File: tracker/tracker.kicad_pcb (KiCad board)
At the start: 4 copper layers, 49.4 x 53.2 mm, 88 parts, among them J1 Conn_01x01, J2 Conn_01x01, J3 Conn_01x05, J4 Conn_Coaxial, J5 SIM_Card, J6 Conn_01x02, M1 BG96, Q1 DMP2008UFG, U1 STM32U545CEUx, U10 PUMH10,115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

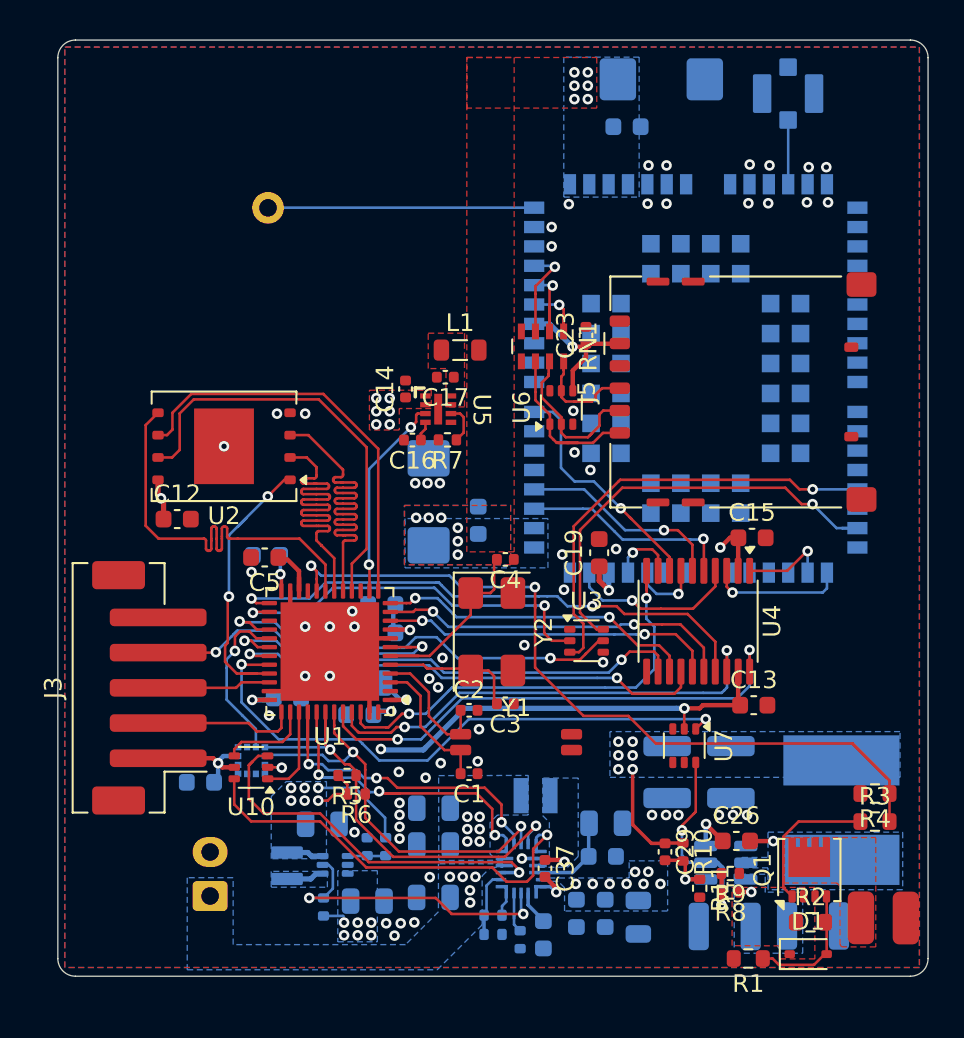
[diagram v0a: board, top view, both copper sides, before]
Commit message: edit silkscreen
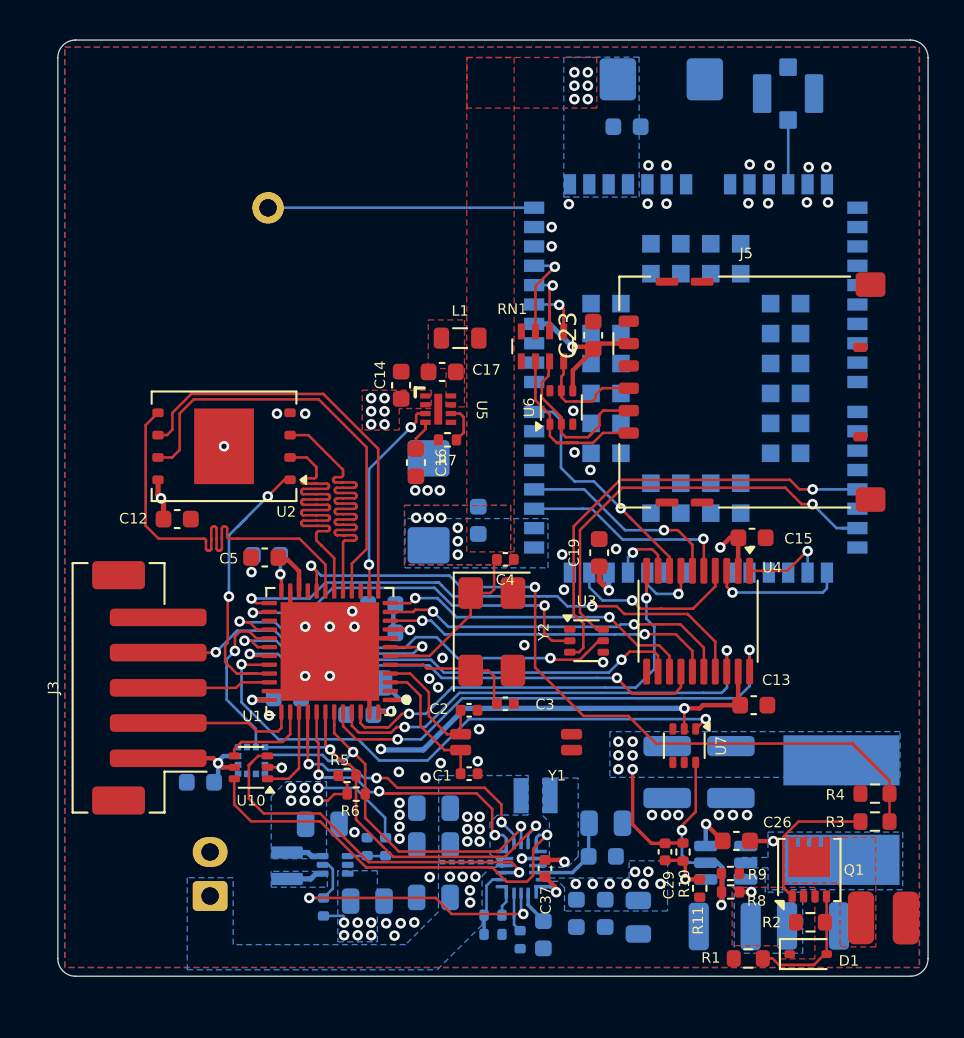
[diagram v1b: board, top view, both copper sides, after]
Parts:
- C14, C16, C17, C23: footprint Capacitor_SMD:C_0402_1005Metric -> Capacitor_SMD:C_0603_1608Metric
- moved C16 1.30 mm to (142.9, 67.4), turned to -90 degrees
- moved L1 0.68 mm to (145.4, 60.3)
- moved J5 0.51 mm to (161.6, 63.4)
- moved C23 0.41 mm to (153.0, 60.1)
- moved C17 0.35 mm to (144.4, 62.2)
- moved C14 0.33 mm to (142.1, 63.0)
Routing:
- net Net-(U5-SS): track 1.11 -> 2.11 mm

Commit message: edits
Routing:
- net /mcu/VIN_MEAS: track 47.2 -> 44.2 mm
- net /battery charger/CHARGER_INT: track 19.6 -> 17.4 mm
- net /mcu/OSC_OUT: track 11.7 -> 10.1 mm
- net /gsm/SIM_IO: track 5.23 -> 3.75 mm
- net /battery charger/CHARGER_STAT: track 18.7 -> 17.3 mm
- net Net-(J5-CLK): track 10.2 -> 8.95 mm
- net /I2C_SCL: track 25.3 -> 24.0 mm
- net /gsm/GSM_LINE_BUF_EN: track 25.7 -> 24.6 mm
- net /gsm/SIM_RST: track 4.02 -> 3.04 mm
- net /mcu/OCTOSPI1_NCS: track 16.7 -> 15.8 mm
- net /mcu/VCAP: track 2.86 -> 2.08 mm
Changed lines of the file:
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@@
 	)
 	(paper "A4")
+	(title_block
+		(date "2025-10-27")
+	)
 	(layers
 		(0 "F.Cu" signal)
@@
 		(tags "resistor")
 		(property "Reference" "R7"
-			(at 0 -1.17 0)
+			(at -1.46 -0.13 0)
 			(layer "F.SilkS")
 			(effects
@@
 		(tags "capacitor")
 		(property "Reference" "C23"
-			(at 0 -1.43 90)
+			(at 1.26 -0.91 90)
 			(layer "F.SilkS")
 			(effects
 				(font
-					(size 1 1)
+					(size 0.6 0.6)
 					(thickness 0.15)
 				)
@@
 		(tags "capacitor")
 		(property "Reference" "C16"
-			(at 0 -1.43 90)
+			(at 0 1.08 90)
 			(layer "F.SilkS")
 			(effects
@@
 		(tags "connector JST PH vertical")
 		(property "Reference" "J3"
-			(at 0 -5.45 90)
+			(at 7.905 -3.44 180)
 			(layer "F.SilkS")
 			(effects
@@
 		(tags "capacitor")
 		(property "Reference" "C4"
-			(at 0 -1.16 0)
+			(at -0.112 0.998 0)
 			(layer "F.SilkS")
 			(effects
@@
 		(tags "Inductor")
 		(property "Reference" "L2"
-			(at 0.1 5.4 90)
+			(at 5.16 0.41 180)
 			(layer "B.SilkS")
 			(effects
@@
 	)
 	(segment
-		(start 141.4375 78.3625)
-		(end 143.05 78.3625)
-		(width 0.15)
-		(layer "F.Cu")
-		(net 5)
-	)
-	(segment
 		(start 147.33 73.04)
 		(end 147.33 74.58)
@@
 	)
 	(segment
-		(start 142.34 77.8625)
-		(end 142.6375 77.8625)
-		(width 0.15)
-		(layer "F.Cu")
-		(net 12)
-	)
-	(segment
 		(start 131.5 78.175)
 		(end 131.525 78.15)
@@
 	(segment
 		(start 150.48 59.93)
-		(end 150.48 58.45)
-		(width 0.15)
-		(layer "F.Cu")
-		(net 17)
-	)
-	(segment
-		(start 150.48 59.93)
 		(end 150.48 57.5)
 		(width 0.15)
@@
 	)
 	(segment
-		(start 155.05 70.5)
-		(end 155.125 70.575)
-		(width 0.15)
-		(layer "F.Cu")
-		(net 34)
-	)
-	(segment
 		(start 154.525 69.975)
 		(end 155.05 70.5)
@@
 	(segment
 		(start 158.16 71.75)
-		(end 158.47 71.75)
-		(width 0.15)
-		(layer "B.Cu")
-		(net 45)
-	)
-	(segment
-		(start 158.16 71.75)
 		(end 159.18 71.75)
 		(width 0.15)
@@
 	(segment
 		(start 151.28 59.93)
-		(end 151.28 58.954166)
-		(width 0.15)
-		(layer "F.Cu")
-		(net 75)
-	)
-	(segment
-		(start 151.28 59.93)
 		(end 151.28 58.672)
 		(width 0.15)
@@
 	)
 	(segment
-		(start 169.65 85.3)
-		(end 167.69 83.34)
-		(width 0.15)
-		(layer "F.Cu")
-		(net 86)
-	)
-	(segment
 		(start 156.52 83.34)
 		(end 154.95 81.77)
@@
 	)
 	(segment
-		(start 149.66 75.63)
-		(end 149.66 75.45)
-		(width 0.15)
-		(layer "F.Cu")
-		(net 86)
-	)
-	(segment
 		(start 149.66 74.7)
 		(end 149.64 74.68)
@@
 	)
 	(segment
-		(start 133.55 79.3625)
-		(end 133.2875 79.3625)
-		(width 0.15)
-		(layer "F.Cu")
-		(net 89)
-	)
-	(segment
 		(start 132.051 78.701)
 		(end 132.051 77.77)
@@
 	)
 	(segment
-		(start 132.775 71.025)
-		(end 133.25 70.55)
-		(width 0.15)
-		(layer "B.Cu")
-		(net 89)
-	)
-	(segment
 		(start 132.27 74.99)
 		(end 132.27 71.505)
@@
 	)
 	(segment
-		(start 137.51 72.07)
-		(end 137.54 72.1)
-		(width 0.15)
-		(layer "F.Cu")
-		(net 91)
-	)
-	(segment
 		(start 137.24 69.175015)
 		(end 136.5 69.175015)
@@
 	)
 	(segment
-		(start 145.08 76.05)
-		(end 144.96 75.93)
-		(width 0.15)
-		(layer "B.Cu")
-		(net 100)
-	)
-	(segment
-		(start 144.96 75.93)
-		(end 144.27 75.24)
-		(width 0.15)
-		(layer "B.Cu")
-		(net 100)
-	)
-	(segment
 		(start 145.19 76.16)
-		(end 144.96 75.93)
+		(end 153.88 76.16)
 		(width 0.15)
 		(layer "B.Cu")
@@
 	)
 	(segment
-		(start 144.11 75.08)
-		(end 142.85 75.08)
+		(start 142.85 75.08)
+		(end 144.11 75.08)
 		(width 0.15)
 		(layer "B.Cu")
@@
 	)
 	(segment
-		(start 153.88 76.16)
+		(start 144.11 75.08)
 		(end 145.19 76.16)
 		(width 0.15)
@@
 	)
 	(segment
-		(start 144.27 75.24)
-		(end 144.11 75.08)
-		(width 0.15)
-		(layer "B.Cu")
-		(net 100)
-	)
-	(segment
 		(start 161.845 79.2525)
 		(end 161.845 78.025)
@@
 	(segment
 		(start 155.995 73.5275)
-		(end 155.995 74.63)
-		(width 0.15)
-		(layer "F.Cu")
-		(net 103)
-	)
-	(segment
-		(start 155.995 73.5275)
 		(end 155.995 75.065)
 		(width 0.15)
@@
 	)
 	(segment
-		(start 144.195 74.195)
-		(end 144.024678 74.195)
-		(width 0.15)
-		(layer "B.Cu")
-		(net 104)
-	)
-	(segment
 		(start 156.87 76.57)
 		(end 157.915 76.57)
@@
 	)
 	(segment
-		(start 141.95 86.17)
-		(end 141.16 86.17)
-		(width 0.15)
-		(layer "F.Cu")
-		(net 108)
-	)
-	(segment
 		(start 146.34 86.17)
 		(end 141.95 86.17)
@@
 	)
 	(segment
-		(start 137.73 85.28)
-		(end 138.32 85.28)
-		(width 0.15)
-		(layer "B.Cu")
-		(net 108)
-	)
-	(segment
 		(start 137.36 85.11)
 		(end 137.53 85.28)
@@
 	)
 	(segment
-		(start 136.75 81.55)
-		(end 136.75 83.7)
-		(width 0.15)
-		(layer "F.Cu")
-		(net 110)
-	)
-	(segment
 		(start 141.83 85.85)
 		(end 146.8 85.85)
@@
 	)
 	(segment
-		(start 136.25 74.675)
-		(end 136.25 73.9)
-		(width 0.254)
-		(layer "F.Cu")
-		(net 118)
-	)
-	(segment
 		(start 136.25 73.545)
 		(end 135.575 72.87)
@@
 	)
 	(segment
-		(start 151.895001 63.91)
-		(end 151.98 63.91)
-		(width 0.15)
-		(layer "F.Cu")
-		(net 127)
-	)
-	(segment
 		(start 153.1025 63.5125)
 		(end 153.46 63.155)
@@
 	)
 	(segment
-		(start 150.95 66.26)
-		(end 151.59 66.26)
-		(width 0.15)
-		(layer "F.Cu")
-		(net 129)
-	)
-	(segment
 		(start 150.5 65.2)
 		(end 150.5 64.66)
@@
 	)
 	(segment
-		(start 151.46 66.26)
-		(end 151.59 66.26)
-		(width 0.15)
-		(layer "F.Cu")
-		(net 129)
-	)
-	(segment
 		(start 150.5 65.87)
 		(end 150.7 66.07)
@@
 	)
 	(segment
-		(start 151.59 66.26)
-		(end 152.08 66.26)
-		(width 0.15)
-		(layer "F.Cu")
-		(net 129)
-	)
-	(segment
 		(start 152.08 66.26)
 		(end 152.95 66.26)
@@
 	)
 	(segment
-		(start 137.75 82.81)
-		(end 137.75 81.55)
-		(width 0.15)
-		(layer "F.Cu")
-		(net 132)
-	)
-	(segment
 		(start 149.71 88.01)
 		(end 147.945 89.775)
@@
 	)
 	(segment
-		(start 148.463 93.11)
-		(end 148.463 93.287)
-		(width 0.15)
-		(layer "B.Cu")
-		(net 137)
-	)
-	(segment
 		(start 148.463 93.623)
 		(end 148.81 93.97)
@@
 	)
 	(segment
-		(start 133.4 86.47)
-		(end 133.4 84.57)
+		(start 133.4 84.57)
+		(end 133.93 84.04)
 		(width 0.15)
 		(layer "F.Cu")
@@
 	)
 	(segment
-		(start 133.93 84.04)
+		(start 133.4 86.47)
 		(end 133.4 84.57)
 		(width 0.15)
@@
 		(width 0.15)
 		(layer "F.Cu")
-		(net 144)
-	)
-	(segment
-		(start 133.62 84.35)
-		(end 133.4 84.57)
-		(width 0.15)
-		(layer "F.Cu")

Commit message: edits
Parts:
- moved J2 0.23 mm to (170.5, 93.2)
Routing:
- net GND: vias 62 -> 326
- added copper zone on In1.Cu, net GND
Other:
- board size 49.4 x 53.2 mm -> 49.4 x 53.4 mm

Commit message: Edits
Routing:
- net GND: track 17.8 -> 19.4 mm, vias 326 -> 335
